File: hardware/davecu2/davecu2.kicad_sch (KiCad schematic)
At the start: 0 parts

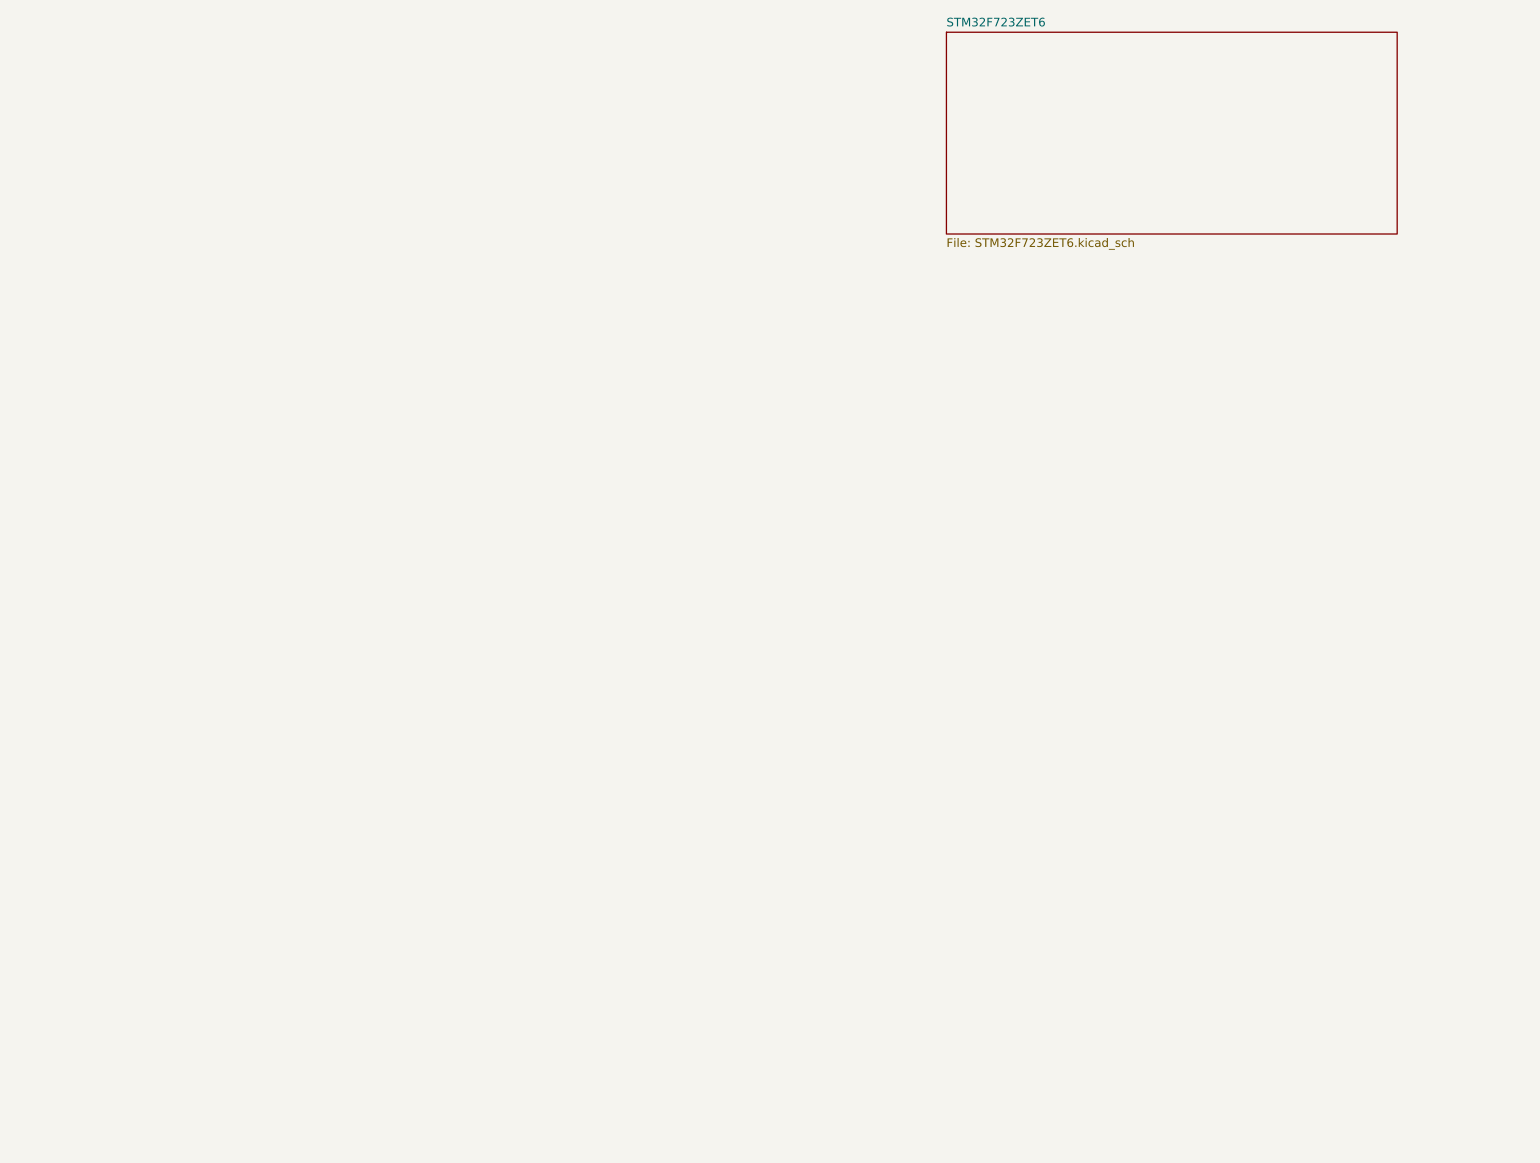
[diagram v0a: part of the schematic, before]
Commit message: add analog input filtering and protection
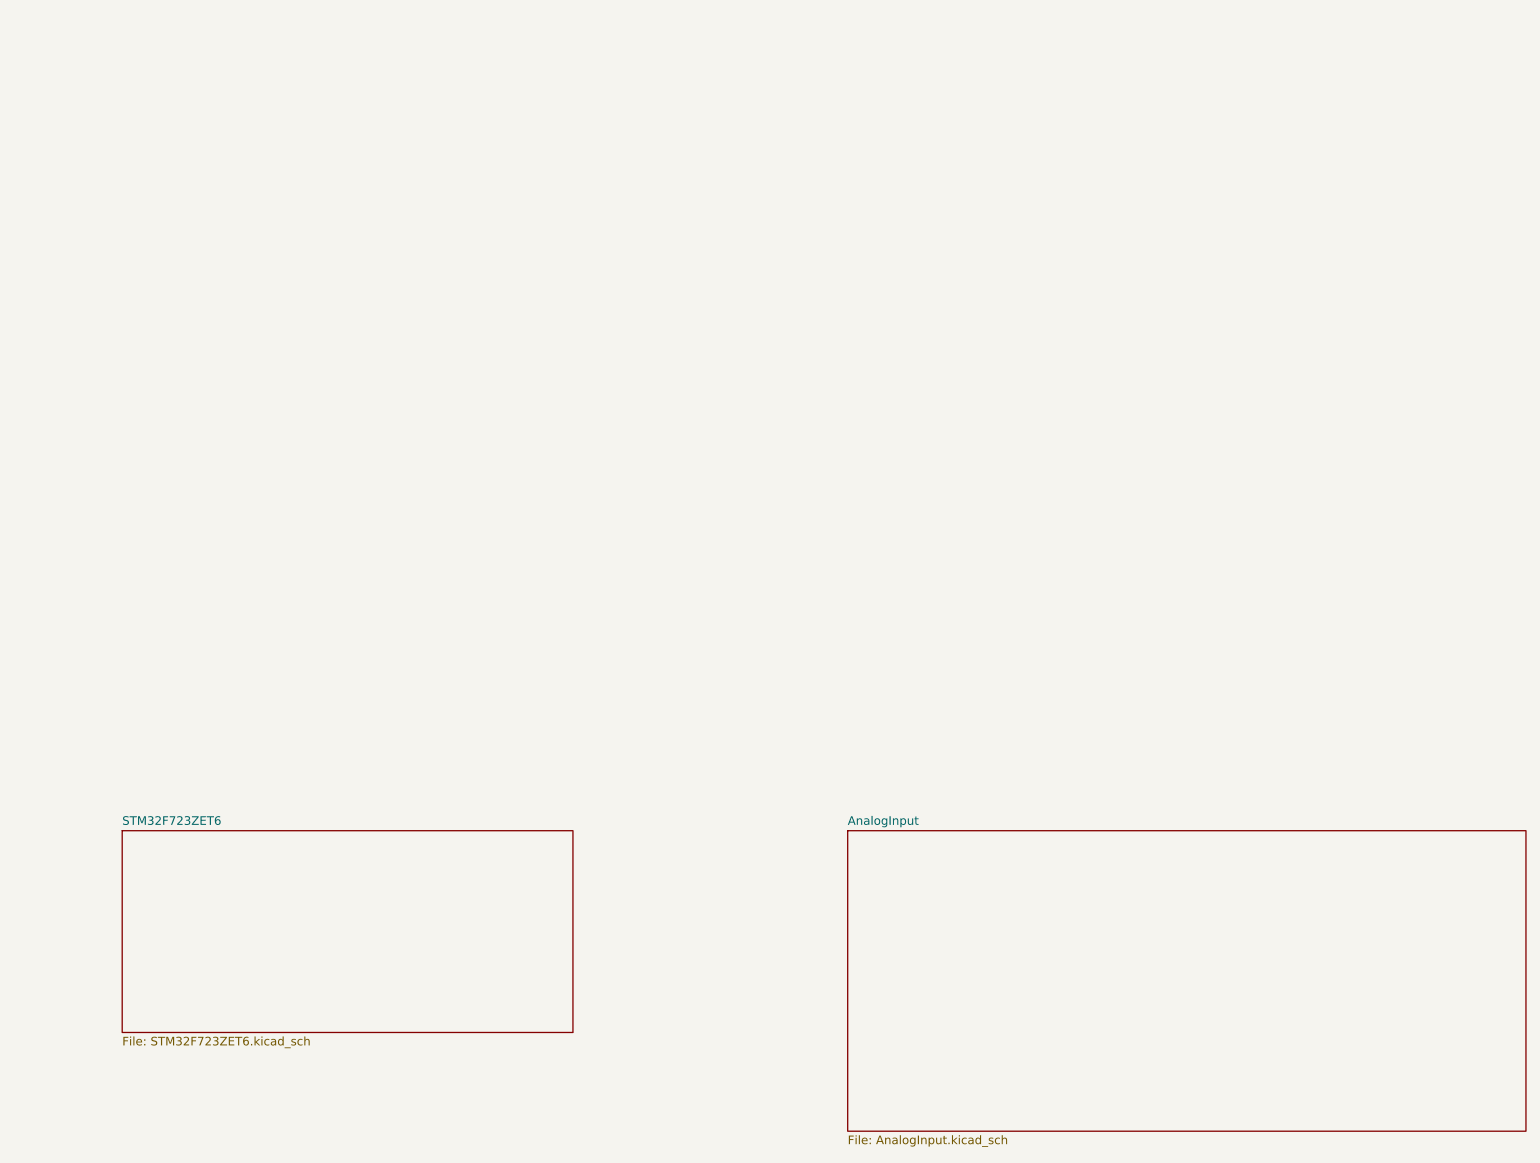
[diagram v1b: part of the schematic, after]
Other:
- added sheet AnalogInput (AnalogInput.kicad_sch)
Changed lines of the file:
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@@
     (comment 1 "https://github.com/miata-bot/can-link")
   )
-  (sheet (at 259.715 -34.29) (size 66.675 29.845) (fields_autoplaced)
+  (sheet (at 245.11 83.82) (size 100.33 44.45) (fields_autoplaced)
     (stroke (width 0.1524) (type solid) (color 0 0 0 0))
     (fill (color 0 0 0 0.0000))
-    (property "Sheet name" "STM32F723ZET6" (id 0) (at 259.715 -35.0016 0)
+    (property "Sheet name" "AnalogInput" (id 0) (at 245.11 83.1084 0)
       (effects (font (size 1.27 1.27)) (justify left bottom))
     )
-    (property "Sheet file" "STM32F723ZET6.kicad_sch" (id 1) (at 259.715 -3.8604 0)
+    (property "Sheet file" "AnalogInput.kicad_sch" (id 1) (at 245.11 128.8546 0)
+      (effects (font (size 1.27 1.27)) (justify left top))
+    )
+  )
+  (sheet (at 137.795 83.82) (size 66.675 29.845) (fields_autoplaced)
+    (stroke (width 0.1524) (type solid) (color 0 0 0 0))
+    (fill (color 0 0 0 0.0000))
+    (property "Sheet name" "STM32F723ZET6" (id 0) (at 137.795 83.1084 0)
+      (effects (font (size 1.27 1.27)) (justify left bottom))
+    )
+    (property "Sheet file" "STM32F723ZET6.kicad_sch" (id 1) (at 137.795 114.2496 0)
       (effects (font (size 1.27 1.27)) (justify left top))
     )
@@
     (path "/" (page "1"))
     (path "/ba06c81d-86b2-46a1-b52c-6637a341b4a7" (page "4"))
+    (path "/0c98809c-a692-42d0-93f2-681cf2e2d1a0" (page "5"))
     (path "/f5becad4-435f-4c1a-8fa2-8b2b4ba75dd3" (page "8"))
     (path "/cdfd05b1-ba4c-4be9-bca4-ea35e57e89e1" (page "9"))
@@
       (reference "#PWR069") (unit 1) (value "GND") (footprint "")
     )
+    (path "/0c98809c-a692-42d0-93f2-681cf2e2d1a0/0157550e-5dba-4450-831e-3bf9b128999f"
+      (reference "#PWR?") (unit 1) (value "GND") (footprint "")
+    )
     (path "/ba06c81d-86b2-46a1-b52c-6637a341b4a7/0199596b-6469-4a80-b406-b6b728170acc"
       (reference "#PWR?") (unit 1) (value "GND") (footprint "")
@@
       (reference "#PWR?") (unit 1) (value "GND") (footprint "")
     )
+    (path "/0c98809c-a692-42d0-93f2-681cf2e2d1a0/0d55d1e4-21b8-4099-9a5b-0e8682840035"
+      (reference "#PWR?") (unit 1) (value "GND") (footprint "")
+    )
+    (path "/0c98809c-a692-42d0-93f2-681cf2e2d1a0/23300274-0c9f-4f93-bacc-4c9bbf9c8a3a"
+      (reference "#PWR?") (unit 1) (value "GND") (footprint "")
+    )
+    (path "/0c98809c-a692-42d0-93f2-681cf2e2d1a0/25cbd818-d518-493f-9a2c-e0cf8971fbc1"
+      (reference "#PWR?") (unit 1) (value "GND") (footprint "")
+    )
+    (path "/0c98809c-a692-42d0-93f2-681cf2e2d1a0/2a9bf6ab-a35b-4387-8e0d-5ccc0d8d7003"
+      (reference "#PWR?") (unit 1) (value "GND") (footprint "")
+    )
+    (path "/0c98809c-a692-42d0-93f2-681cf2e2d1a0/3cdb456b-b5ff-4e17-8fe4-36ed86cde4f6"
+      (reference "#PWR?") (unit 1) (value "GND") (footprint "")
+    )
     (path "/ba06c81d-86b2-46a1-b52c-6637a341b4a7/3dcdcf54-5102-4456-9db0-70983ae9ed1e"
       (reference "#PWR?") (unit 1) (value "GND") (footprint "")
@@
       (reference "#PWR?") (unit 1) (value "GND") (footprint "")
     )
+    (path "/0c98809c-a692-42d0-93f2-681cf2e2d1a0/7c5643a2-7bc9-4e8a-bc07-0aa4e333e782"
+      (reference "#PWR?") (unit 1) (value "GND") (footprint "")
+    )
     (path "/ba06c81d-86b2-46a1-b52c-6637a341b4a7/7fc75bb5-3e2f-4e03-bfd9-8eb6829449f6"
       (reference "#PWR?") (unit 1) (value "GND") (footprint "")
     )
+    (path "/0c98809c-a692-42d0-93f2-681cf2e2d1a0/95be1708-3f01-4cbe-a4db-fea108eec5f4"
+      (reference "#PWR?") (unit 1) (value "GND") (footprint "")
+    )
+    (path "/0c98809c-a692-42d0-93f2-681cf2e2d1a0/9dfdc515-ed16-4541-bcdd-3c135399b64f"
+      (reference "#PWR?") (unit 1) (value "GND") (footprint "")
+    )
     (path "/ba06c81d-86b2-46a1-b52c-6637a341b4a7/a31fa726-e3e3-47b8-b790-b5d94202beef"
       (reference "#PWR?") (unit 1) (value "GND") (footprint "")
     )
+    (path "/0c98809c-a692-42d0-93f2-681cf2e2d1a0/a42273d7-60ec-451e-a388-33b5e3e76274"
+      (reference "#PWR?") (unit 1) (value "GND") (footprint "")
+    )
+    (path "/0c98809c-a692-42d0-93f2-681cf2e2d1a0/a52cdb39-34ff-4bb9-abae-b9f222bfc819"
+      (reference "#PWR?") (unit 1) (value "GND") (footprint "")
+    )
     (path "/ba06c81d-86b2-46a1-b52c-6637a341b4a7/b083d4dc-330f-4ebb-b248-4936d671f309"
       (reference "#PWR?") (unit 1) (value "GND") (footprint "")
     )
     (path "/ba06c81d-86b2-46a1-b52c-6637a341b4a7/d639e7bb-ce58-40a7-89df-ff724683e47b"
+      (reference "#PWR?") (unit 1) (value "GND") (footprint "")
+    )
+    (path "/0c98809c-a692-42d0-93f2-681cf2e2d1a0/d7f98b92-d890-4b24-a180-2118093da6e2"
       (reference "#PWR?") (unit 1) (value "GND") (footprint "")
     )
@@
       (reference "C?") (unit 1) (value "1uF") (footprint "Capacitor_SMD:C_0805_2012Metric")
     )
+    (path "/0c98809c-a692-42d0-93f2-681cf2e2d1a0/0f1f3190-64a3-4c19-a165-3a72cef5ab25"
+      (reference "C?") (unit 1) (value "1uF") (footprint "")
+    )
     (path "/ba06c81d-86b2-46a1-b52c-6637a341b4a7/1ef6f521-1062-480c-abca-8bf34217e00f"
       (reference "C?") (unit 1) (value "100nF") (footprint "Capacitor_SMD:C_0402_1005Metric")
@@
       (reference "C?") (unit 1) (value "100nF") (footprint "Capacitor_SMD:C_0402_1005Metric")
     )
+    (path "/0c98809c-a692-42d0-93f2-681cf2e2d1a0/68816921-3419-44ca-bcc5-ea7837015a15"
+      (reference "C?") (unit 1) (value "1uF") (footprint "")
+    )
     (path "/ba06c81d-86b2-46a1-b52c-6637a341b4a7/6eab57d1-2342-4a47-970a-0dbae974c9d5"
       (reference "C?") (unit 1) (value "2.2nF") (footprint "Capacitor_SMD:C_0402_1005Metric")
     )
+    (path "/0c98809c-a692-42d0-93f2-681cf2e2d1a0/796cc4bf-e196-42cb-9a05-f2d1c3d73c81"
+      (reference "C?") (unit 1) (value "1uF") (footprint "")
+    )
     (path "/ba06c81d-86b2-46a1-b52c-6637a341b4a7/7d41af8f-41cd-40cc-ae35-188541a2822d"
       (reference "C?") (unit 1) (value "4.7uF") (footprint "Capacitor_SMD:C_0805_2012Metric")
@@
       (reference "C?") (unit 1) (value "100nF") (footprint "Capacitor_SMD:C_0402_1005Metric")
     )
+    (path "/0c98809c-a692-42d0-93f2-681cf2e2d1a0/fca88466-9c0a-4071-aca2-6efe14500ca4"
+      (reference "C?") (unit 1) (value "1uF") (footprint "")
+    )
     (path "/ba06c81d-86b2-46a1-b52c-6637a341b4a7/fcef263d-69a6-45d3-b409-48cd8c02e1c1"
       (reference "C?") (unit 1) (value "2.2nF") (footprint "Capacitor_SMD:C_0402_1005Metric")
@@
       (reference "D4") (unit 1) (value "D_Schottky_Small") (footprint "Diode_SMD:D_SMA")
     )
+    (path "/0c98809c-a692-42d0-93f2-681cf2e2d1a0/1ce5cfba-7e45-47c4-9ffb-340154983854"
+      (reference "D?") (unit 1) (value "D_Schottky_Small") (footprint "")
+    )
+    (path "/0c98809c-a692-42d0-93f2-681cf2e2d1a0/435b1159-3910-4c20-abde-77defceaad63"
+      (reference "D?") (unit 1) (value "D_Schottky_Small") (footprint "")
+    )
+    (path "/0c98809c-a692-42d0-93f2-681cf2e2d1a0/5dd72619-8865-48e4-9299-1cf68e59fd77"
+      (reference "D?") (unit 1) (value "D_Schottky_Small") (footprint "")
+    )
+    (path "/0c98809c-a692-42d0-93f2-681cf2e2d1a0/97eb45fa-745f-4e8b-87e3-d78041cc0269"
+      (reference "D?") (unit 1) (value "D_Schottky_Small") (footprint "")
+    )
     (path "/ba06c81d-86b2-46a1-b52c-6637a341b4a7/681106c8-0824-4906-a59d-e1e841a7d244"
       (reference "FB?") (unit 1) (value "FerriteBead_Small") (footprint "")
@@
       (reference "R?") (unit 1) (value "10k") (footprint "Resistor_SMD:R_0402_1005Metric")
     )
+    (path "/0c98809c-a692-42d0-93f2-681cf2e2d1a0/2b88bf21-8e83-466b-9763-6b172b4e2d82"
+      (reference "R?") (unit 1) (value "16k") (footprint "")
+    )
+    (path "/0c98809c-a692-42d0-93f2-681cf2e2d1a0/3602ab2d-cbfa-43e8-84a8-b01a41a11ec2"
+      (reference "R?") (unit 1) (value "47k") (footprint "")
+    )
+    (path "/0c98809c-a692-42d0-93f2-681cf2e2d1a0/443ddb09-198f-469c-ab97-40ccb18a9b13"
+      (reference "R?") (unit 1) (value "47k") (footprint "")
+    )
+    (path "/0c98809c-a692-42d0-93f2-681cf2e2d1a0/4e4c13d8-0a01-49c9-a795-a1d30ff9efd2"
+      (reference "R?") (unit 1) (value "16k") (footprint "")
+    )
+    (path "/0c98809c-a692-42d0-93f2-681cf2e2d1a0/73e5534a-54c5-4262-b01f-23bc078491b7"
+      (reference "R?") (unit 1) (value "16k") (footprint "")
+    )
+    (path "/0c98809c-a692-42d0-93f2-681cf2e2d1a0/868f7df6-b844-400b-b219-f5c49af68b01"
+      (reference "R?") (unit 1) (value "47k") (footprint "")
+    )
     (path "/ba06c81d-86b2-46a1-b52c-6637a341b4a7/a55ba9df-000b-4ffe-94e5-684fe0ee777f"
       (reference "R?") (unit 1) (value "10k") (footprint "Resistor_SMD:R_0402_1005Metric")
     )
+    (path "/0c98809c-a692-42d0-93f2-681cf2e2d1a0/c6006ca9-6bdd-4265-935b-4ec1eaa3c88a"
+      (reference "R?") (unit 1) (value "16k") (footprint "")
+    )
     (path "/ba06c81d-86b2-46a1-b52c-6637a341b4a7/cc90535c-6f17-4e09-b097-8be4c394494f"
       (reference "R?") (unit 1) (value "3k") (footprint "Resistor_SMD:R_0402_1005Metric")
     )
+    (path "/0c98809c-a692-42d0-93f2-681cf2e2d1a0/f8b6bb9f-ad03-4bcb-9251-2a066978a098"
+      (reference "R?") (unit 1) (value "47k") (footprint "")
+    )
     (path "/ba06c81d-86b2-46a1-b52c-6637a341b4a7/a348e561-47c5-4cc4-8a47-bc7ff0938eb6"

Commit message: schematic cleanup
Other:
- added sheet Connectors (Connectors.kicad_sch)
- added sheet Wideband (Wideband.kicad_sch)
- sheet AnalogInput ports: added APP1_IN, APP1_OUT, APP2_IN, APP2_OUT, APV_ANGLE_IN, APV_ANGLE_OUT, BARO_IN, BARO_OUT, CLT_LEVEL_IN, CLT_LEVEL_OUT, ECT_IN, ECT_OUT, IAT_IN, IAT_OUT, KNOCK_IN, KNOCK_OUT, MAF_IN, MAF_OUT, TPS1_IN, TPS1_OUT, TPS2_IN, TPS2_OUT, VBATT, VSENSE_OUT; removed none
- sheet CAN-Bus ports: added CAN_EN, CAN_RX, CAN_TX, VDD; removed EN, GPIO_CAN_N, GPIO_CAN_P
- sheet Power ports: added VDD; removed VSENSE
- sheet STM32F723ZET6 ports: added AC_LOAD_SW, AC_RELAY, AIR_PUMP_RELAY, AIR_SOLENOID, APP1, APP2, APV_ANGLE, APV_MOTOR_+, APV_MOTOR_-, BARO, CAN_RX, CAN_TX, CLT_LEVEL, CRUISE_SW, DBW_MOTOR_+, DBW_MOTOR_-, DBW_RELAY, ECT, ESHAFT, FAN_RELAY1, FAN_RELAY2, FRONT_O2_HEATER, FUEL_PUMP_RELAY1, FUEL_PUMP_RELAY2, IAT, IGN_FRONT_LEADING, IGN_FRONT_TRAILING, IGN_REAR_LEADING, IGN_REAR_TRAILING, IGN_RELAY, INJECTOR_FRONT_PRIMARY1, INJECTOR_FRONT_PRIMARY2, INJECTOR_FRONT_SECONDARY, INJECTOR_REAR_PRIMARY1, INJECTOR_REAR_PRIMARY2, INJECTOR_REAR_SECONDARY, KNOCK, MAF, MAIN_RELAY, OIL_LEVEL_SW, OIL_PRESSURE_SW, OMP_1, OMP_2, OMP_3, OMP_4, OMP_SW, PURGE_SOLENOID, REAR_O2_HEATER, SPI1_MISO, SPI1_MOSI, SPI1_NSS1, SPI1_NSS2, SPI1_SCK, SSV_CTRL, SSV_SW, STARTER_RELAY, TACH, THROTTLE_POSITION_1, THROTTLE_POSITION_2, UART4_RX, UART4_TX, USB_DN, USB_DP, VDD, VDI_SOLENOID, VFAD_SOLENOID; removed none
